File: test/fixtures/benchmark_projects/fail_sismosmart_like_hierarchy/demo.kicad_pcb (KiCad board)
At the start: 60 x 40 mm, 0 parts

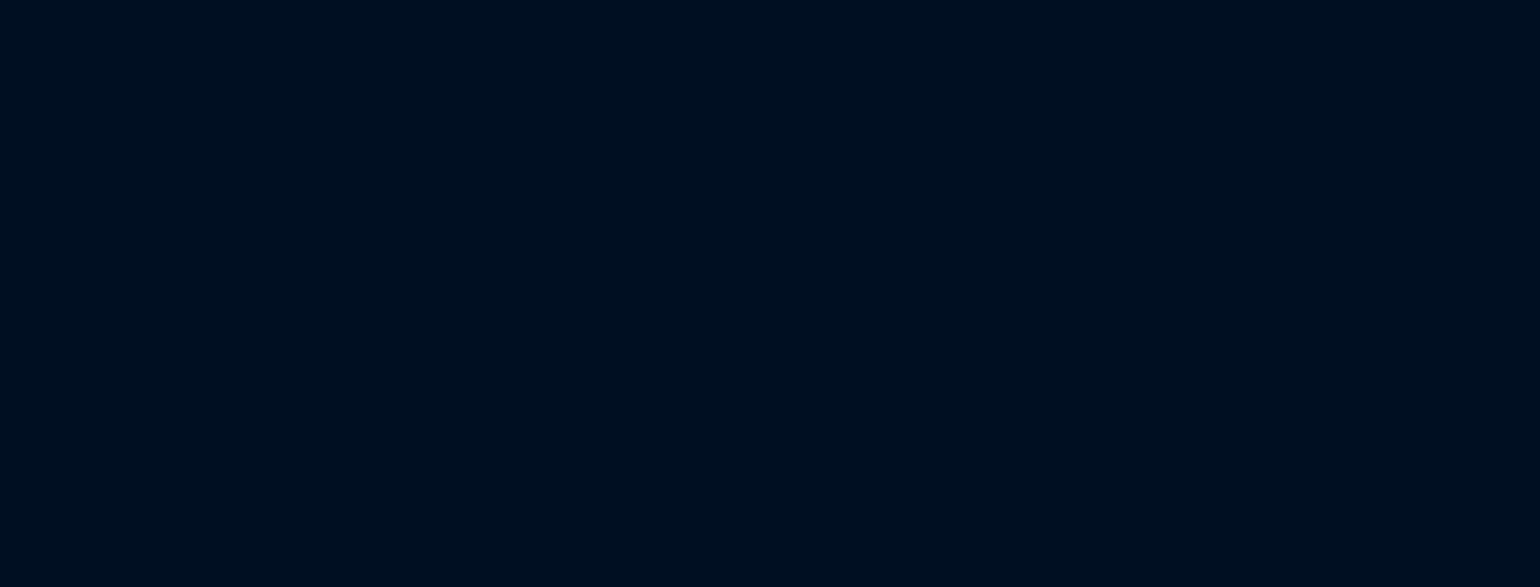
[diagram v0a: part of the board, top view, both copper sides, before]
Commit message: test(fixtures): clean up and fix benchmark project fixtures
- Remove 4 empty kicad10_* stub projects (kicad10_variants,
  kicad10_timedomain, kicad10_custom_drc, kicad10_design_blocks)
  that had no schematic/PCB content and were not referenced by any test
- Remove stray demo.kicad_prl from fail_bad_decoupling_placement
- Fix 3 fail_* projects whose schematics were empty while PCBs had
  content (fail_bad_decoupling_placement, fail_dfm_edge_clearance,
  fail_sensor_cluster_spread): add matching component symbols
- Fix 3 fail_* projects whose PCBs were empty while schematics had
  content (fail_label_only_schematic, fail_sismosmart_like_hierarchy,
  fail_sismosmart_like_label_only): add matching footprints

All 10 remaining fixtures now have consistent schematic + PCB content
that matches their intended failure scenario.
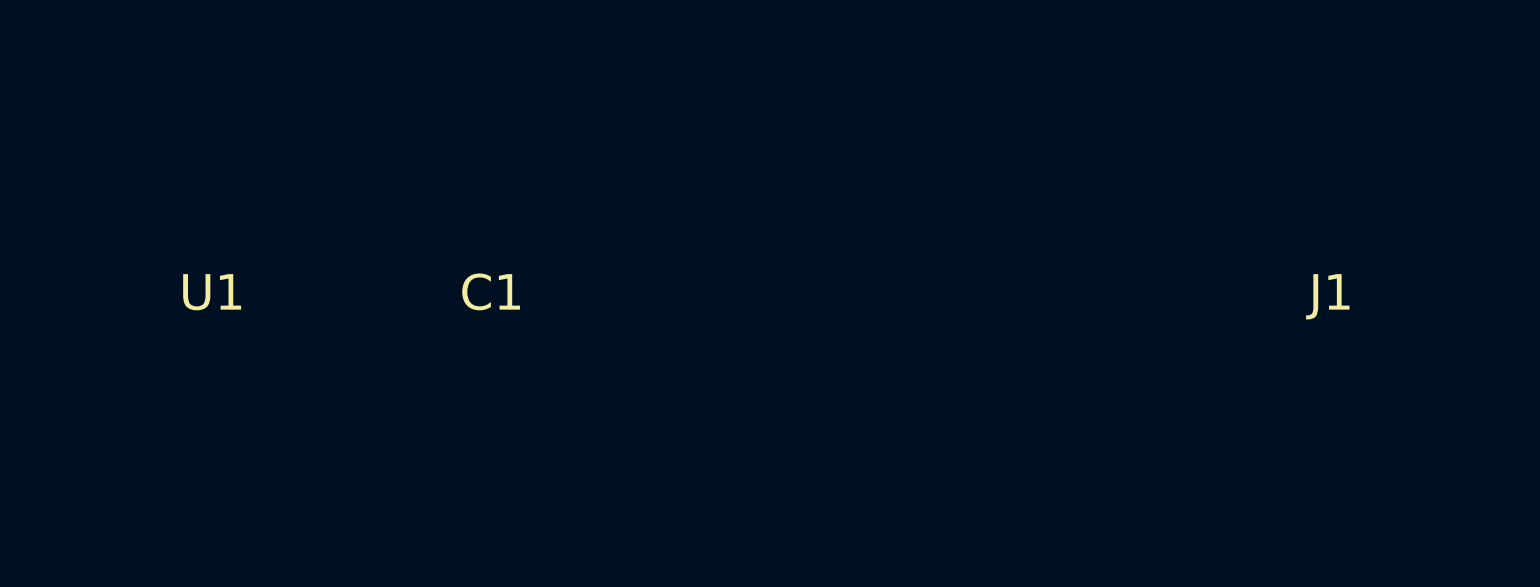
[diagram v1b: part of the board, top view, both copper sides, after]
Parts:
- added C1: 10u, Capacitor_SMD:C_0805, F.Cu at (20.0, 20.0)
- added J1: VOUT, Connector_Generic:Conn_01x02, F.Cu at (50.0, 20.0)
- added U1: PowerReg, Regulator_Linear:LM7805_TO220, F.Cu at (10.0, 20.0)
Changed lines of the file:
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@@
   (generator "pytest")
   (gr_rect (start 0 0) (end 60 40) (stroke (width 0.05) (type solid)) (fill no) (layer "Edge.Cuts"))
+  (footprint "Regulator_Linear:LM7805_TO220"
+    (layer "F.Cu")
+    (at 10 20 0)
+    (property "Reference" "U1" (at 0 0 0) (layer "F.SilkS"))
+    (property "Value" "PowerReg" (at 0 3 0) (layer "F.Fab"))
+    (fp_rect (start -3.5 -2) (end 3.5 5) (stroke (width 0.05) (type solid)) (fill no) (layer "F.CrtYd"))
+  )
+  (footprint "Capacitor_SMD:C_0805"
+    (layer "F.Cu")
+    (at 20 20 0)
+    (property "Reference" "C1" (at 0 0 0) (layer "F.SilkS"))
+    (property "Value" "10u" (at 0 1.5 0) (layer "F.Fab"))
+    (fp_rect (start -1.5 -1) (end 1.5 1) (stroke (width 0.05) (type solid)) (fill no) (layer "F.CrtYd"))
+  )
+  (footprint "Connector_Generic:Conn_01x02"
+    (layer "F.Cu")
+    (at 50 20 0)
+    (property "Reference" "J1" (at 0 0 0) (layer "F.SilkS"))
+    (property "Value" "VOUT" (at 0 2 0) (layer "F.Fab"))
+    (fp_rect (start -1.5 -2.5) (end 1.5 2.5) (stroke (width 0.05) (type solid)) (fill no) (layer "F.CrtYd"))
+  )
 )
